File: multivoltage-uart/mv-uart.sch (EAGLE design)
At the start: 39 parts, among them SW1 DIP_SP6T, U1 IP4234CZ6, U2 CP2105-GM, U3 LDO_SHD_ADJ-AP2127K-ADJ, X1 MINI-USB-SHIELD-UX60-MB-5ST

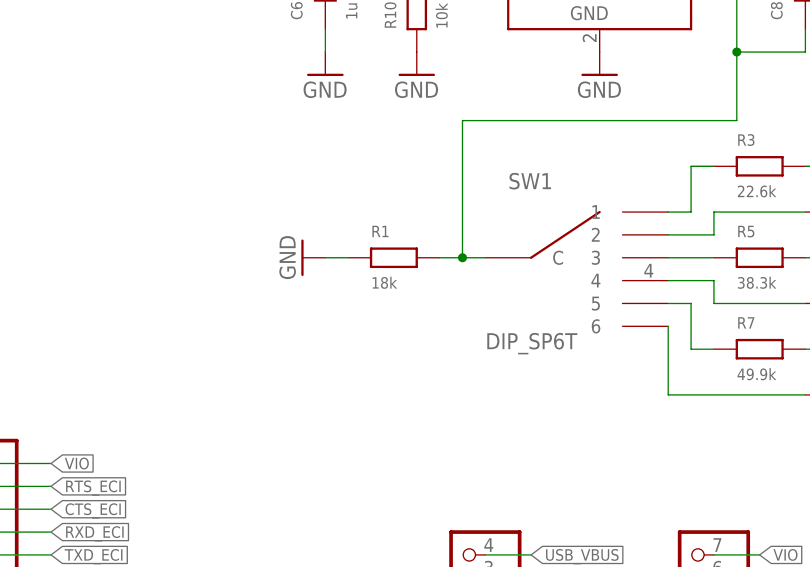
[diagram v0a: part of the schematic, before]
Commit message: mv-uart: Add digikey link for all major parts
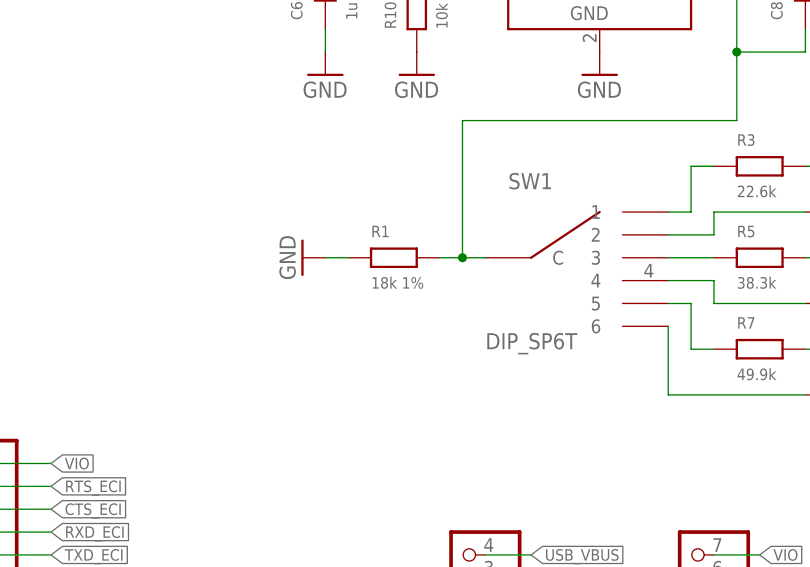
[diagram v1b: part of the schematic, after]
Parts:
- C1, C2, C3, C4, C5, C6, C7, C8, C9: CLASS (none) -> CAPACITOR; DESCRIPTION (none) -> NO DESCRIPTION; LINK (none) -> UNKNOWN LINK; MANUFACTURER (none) -> UNKNOWN MANUFACTURER; MANUFACTURERPARTNUMBER (none) -> UNKNOWN MANUFACTURER PART NUMBER; POPULATED (none) -> TRUE; ROHSCERTIFICATE (none) -> UNKNOWN ROHS CERTIFICATE; SOURCE (none) -> UNKNOWN SOURCE; SOURCEPARTNUMBER (none) -> UNKNOWN SOURCE PART NUMBER
- D1, D2: CLASS (none) -> DIODE; DESCRIPTION (none) -> NO DESCRIPTION; LINK (none) -> http://www.digikey.com/product-detail/en/wurth-electronics-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; MANUFACTURER (none) -> UNKNOWN MANUFACTURER; MANUFACTURERPARTNUMBER (none) -> UNKNOWN MANUFACTURER PART NUMBER; POPULATED (none) -> TRUE; ROHSCERTIFICATE (none) -> UNKNOWN ROHS CERTIFICATE; SOURCE (none) -> UNKNOWN SOURCE; SOURCEPARTNUMBER (none) -> UNKNOWN SOURCE PART NUMBER
- JP1, JP2, JP3, JP4, JP5: CLASS (none) -> CONNECTOR\JUMPER; DESCRIPTION (none) -> NO DESCRIPTION; LINK (none) -> UNKNOWN LINK; MANUFACTURER (none) -> UNKNOWN MANUFACTURER; MANUFACTURERPARTNUMBER (none) -> UNKNOWN MANUFACTURER PART NUMBER; POPULATED (none) -> TRUE; ROHSCERTIFICATE (none) -> UNKNOWN ROHS CERTIFICATE; SOURCE (none) -> UNKNOWN SOURCE; SOURCEPARTNUMBER (none) -> UNKNOWN SOURCE PART NUMBER
- R1: value 18k -> 18k 1%; CLASS (none) -> RESISTOR; DESCRIPTION (none) -> NO DESCRIPTION; LINK (none) -> http://www.digikey.com/product-detail/en/yageo/RC0603FR-071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; MANUFACTURER (none) -> UNKNOWN MANUFACTURER; MANUFACTURERPARTNUMBER (none) -> UNKNOWN MANUFACTURER PART NUMBER; POPULATED (none) -> TRUE; ROHSCERTIFICATE (none) -> UNKNOWN ROHS CERTIFICATE; SOURCE (none) -> UNKNOWN SOURCE; SOURCEPARTNUMBER (none) -> UNKNOWN SOURCE PART NUMBER
- R10, R11, R12, R13, R14, R15, R16, R17, R18, R2, R9: CLASS (none) -> RESISTOR; DESCRIPTION (none) -> NO DESCRIPTION; LINK (none) -> UNKNOWN LINK; MANUFACTURER (none) -> UNKNOWN MANUFACTURER; MANUFACTURERPARTNUMBER (none) -> UNKNOWN MANUFACTURER PART NUMBER; POPULATED (none) -> TRUE; ROHSCERTIFICATE (none) -> UNKNOWN ROHS CERTIFICATE; SOURCE (none) -> UNKNOWN SOURCE; SOURCEPARTNUMBER (none) -> UNKNOWN SOURCE PART NUMBER
- R3: CLASS (none) -> RESISTOR; DESCRIPTION (none) -> NO DESCRIPTION; LINK (none) -> http://www.digikey.com/product-detail/en/yageo/RC0603FR-072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; MANUFACTURER (none) -> UNKNOWN MANUFACTURER; MANUFACTURERPARTNUMBER (none) -> UNKNOWN MANUFACTURER PART NUMBER; POPULATED (none) -> TRUE; ROHSCERTIFICATE (none) -> UNKNOWN ROHS CERTIFICATE; SOURCE (none) -> UNKNOWN SOURCE; SOURCEPARTNUMBER (none) -> UNKNOWN SOURCE PART NUMBER
- R4, R5: CLASS (none) -> RESISTOR; DESCRIPTION (none) -> NO DESCRIPTION; LINK (none) -> http://www.digikey.com/product-detail/en/yageo/RC0603FR-073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; MANUFACTURER (none) -> UNKNOWN MANUFACTURER; MANUFACTURERPARTNUMBER (none) -> UNKNOWN MANUFACTURER PART NUMBER; POPULATED (none) -> TRUE; ROHSCERTIFICATE (none) -> UNKNOWN ROHS CERTIFICATE; SOURCE (none) -> UNKNOWN SOURCE; SOURCEPARTNUMBER (none) -> UNKNOWN SOURCE PART NUMBER
- R6, R7: CLASS (none) -> RESISTOR; DESCRIPTION (none) -> NO DESCRIPTION; LINK (none) -> http://www.digikey.com/product-detail/en/yageo/RC0603FR-074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; MANUFACTURER (none) -> UNKNOWN MANUFACTURER; MANUFACTURERPARTNUMBER (none) -> UNKNOWN MANUFACTURER PART NUMBER; POPULATED (none) -> TRUE; ROHSCERTIFICATE (none) -> UNKNOWN ROHS CERTIFICATE; SOURCE (none) -> UNKNOWN SOURCE; SOURCEPARTNUMBER (none) -> UNKNOWN SOURCE PART NUMBER
- R8: CLASS (none) -> RESISTOR; DESCRIPTION (none) -> NO DESCRIPTION; LINK (none) -> http://www.digikey.com/product-detail/en/yageo/RC0603FR-075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; MANUFACTURER (none) -> UNKNOWN MANUFACTURER; MANUFACTURERPARTNUMBER (none) -> UNKNOWN MANUFACTURER PART NUMBER; POPULATED (none) -> TRUE; ROHSCERTIFICATE (none) -> UNKNOWN ROHS CERTIFICATE; SOURCE (none) -> UNKNOWN SOURCE; SOURCEPARTNUMBER (none) -> UNKNOWN SOURCE PART NUMBER
- SW1: CLASS (none) -> UNKNOWN CLASS; DESCRIPTION (none) -> NO DESCRIPTION; LINK (none) -> UNKNOWN LINK; MANUFACTURER (none) -> UNKNOWN MANUFACTURER; MANUFACTURERPARTNUMBER (none) -> UNKNOWN MANUFACTURER PART NUMBER; POPULATED (none) -> TRUE; ROHSCERTIFICATE (none) -> UNKNOWN ROHS CERTIFICATE; SOURCE (none) -> UNKNOWN SOURCE; SOURCEPARTNUMBER (none) -> UNKNOWN SOURCE PART NUMBER
- U1: CLASS (none) -> IC; DESCRIPTION (none) -> NO DESCRIPTION; LINK (none) -> http://www.digikey.com/product-detail/en/nxp-semiconductors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; MANUFACTURER (none) -> UNKNOWN MANUFACTURER; MANUFACTURERPARTNUMBER (none) -> UNKNOWN MANUFACTURER PART NUMBER; POPULATED (none) -> TRUE; ROHSCERTIFICATE (none) -> UNKNOWN ROHS CERTIFICATE; SOURCE (none) -> UNKNOWN SOURCE; SOURCEPARTNUMBER (none) -> UNKNOWN SOURCE PART NUMBER
- U2: CLASS (none) -> IC; DESCRIPTION (none) -> NO DESCRIPTION; LINK (none) -> http://www.digikey.com/product-detail/en/silicon-labs/CP210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; MANUFACTURER (none) -> UNKNOWN MANUFACTURER; MANUFACTURERPARTNUMBER (none) -> UNKNOWN MANUFACTURER PART NUMBER; POPULATED (none) -> TRUE; ROHSCERTIFICATE (none) -> UNKNOWN ROHS CERTIFICATE; SOURCE (none) -> UNKNOWN SOURCE; SOURCEPARTNUMBER (none) -> UNKNOWN SOURCE PART NUMBER
- U3: CLASS (none) -> IC; DESCRIPTION (none) -> NO DESCRIPTION; LINK (none) -> http://www.digikey.com/product-detail/en/diodes-incorporate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; MANUFACTURER (none) -> UNKNOWN MANUFACTURER; MANUFACTURERPARTNUMBER (none) -> UNKNOWN MANUFACTURER PART NUMBER; POPULATED (none) -> TRUE; ROHSCERTIFICATE (none) -> UNKNOWN ROHS CERTIFICATE; SOURCE (none) -> UNKNOWN SOURCE; SOURCEPARTNUMBER (none) -> UNKNOWN SOURCE PART NUMBER
- X1: CLASS (none) -> CONNECTOR; DESCRIPTION (none) -> NO DESCRIPTION; LINK (none) -> http://www.digikey.com/product-detail/en/hirose-electric-co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; MANUFACTURER (none) -> UNKNOWN MANUFACTURER; MANUFACTURERPARTNUMBER (none) -> UNKNOWN MANUFACTURER PART NUMBER; POPULATED (none) -> TRUE; ROHSCERTIFICATE (none) -> UNKNOWN ROHS CERTIFICATE; SOURCE (none) -> UNKNOWN SOURCE; SOURCEPARTNUMBER (none) -> UNKNOWN SOURCE PART NUMBER

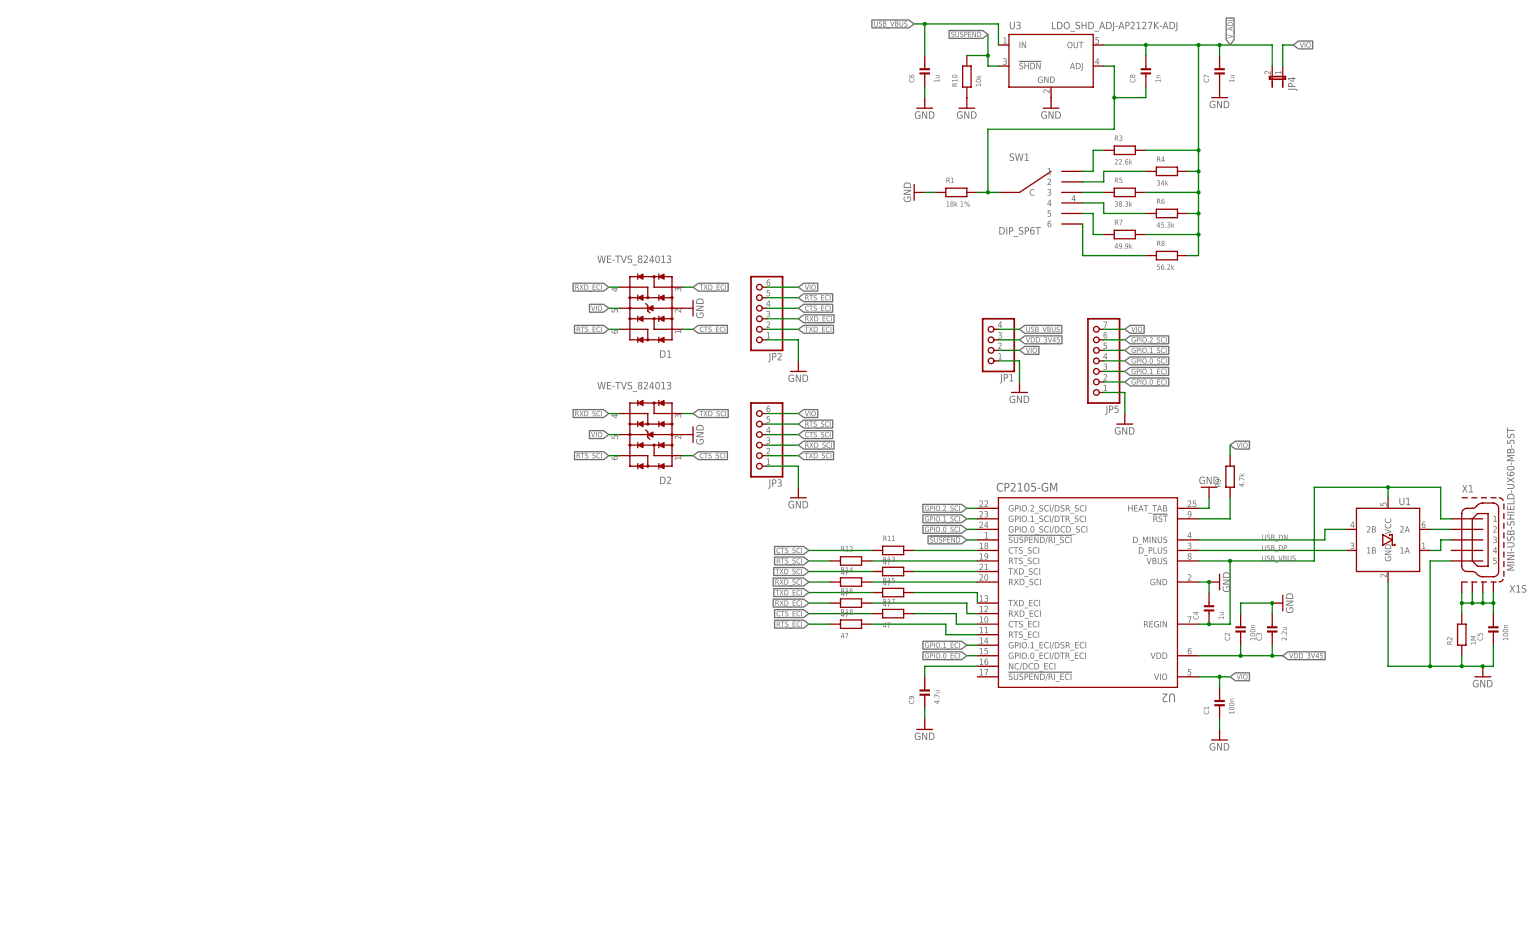
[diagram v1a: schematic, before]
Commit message: mv-uart: Beatify schematics + Add comments
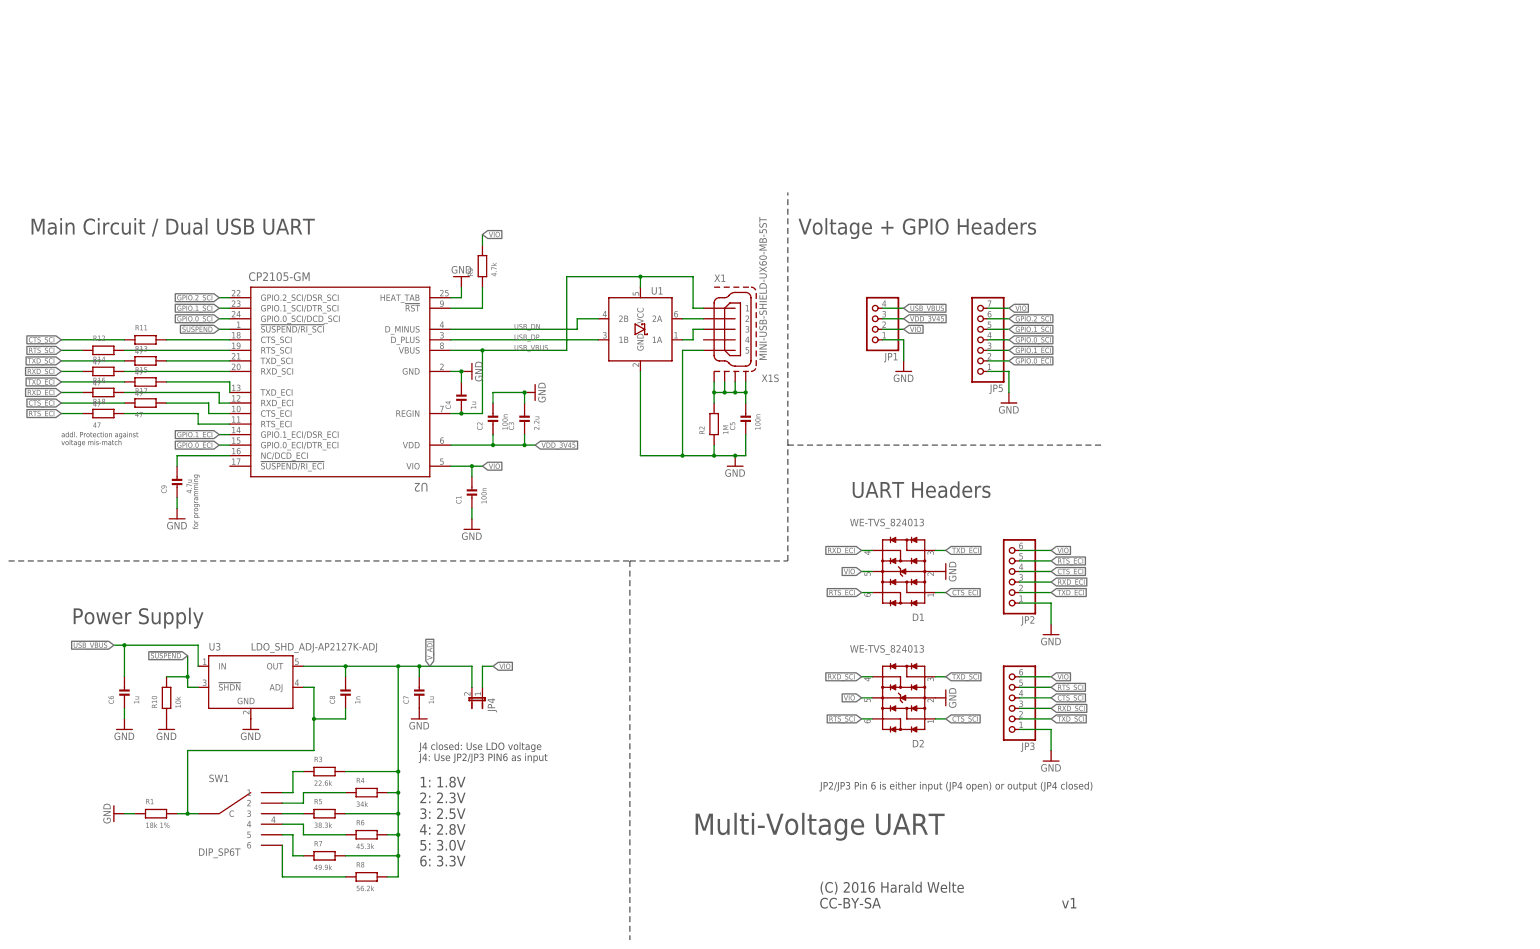
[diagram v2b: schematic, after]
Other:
- note added: "(C) 2016 Harald Welte CC-BY-SA"
- note added: "1: 1.8V 2: 2.3V 3: 2.5V 4: 2.8V 5: 3.0V 6: 3.3V"
- note added: "J4 closed: Use LDO voltage J4: Use JP2/JP3 PIN6 as input"
- note added: "JP2/JP3 Pin 6 is either input (JP4 open) or output (JP4 closed)"
- note added: "Main Circuit / Dual USB UART"
- note added: "Multi-Voltage UART"
- note added: "Power Supply"
- note added: "UART Headers"
- note added: "Voltage + GPIO Headers"
- note added: "addl. Protection against voltage mis-match"
- note added: "for programming"
- moved on the sheet: C1, C2, C3, C4, C5, C6, C7, C8, C9, D1, D2, JP1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

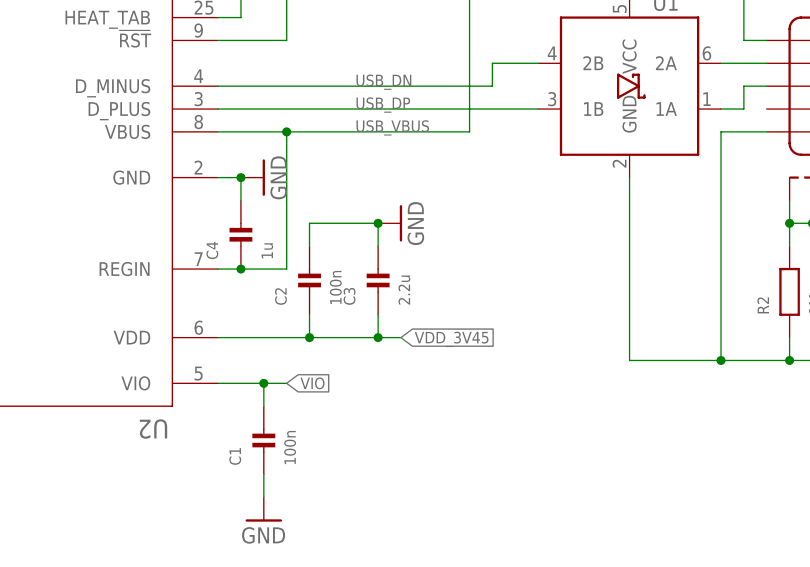
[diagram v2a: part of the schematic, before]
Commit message: Complete BOM attributes + export BOM
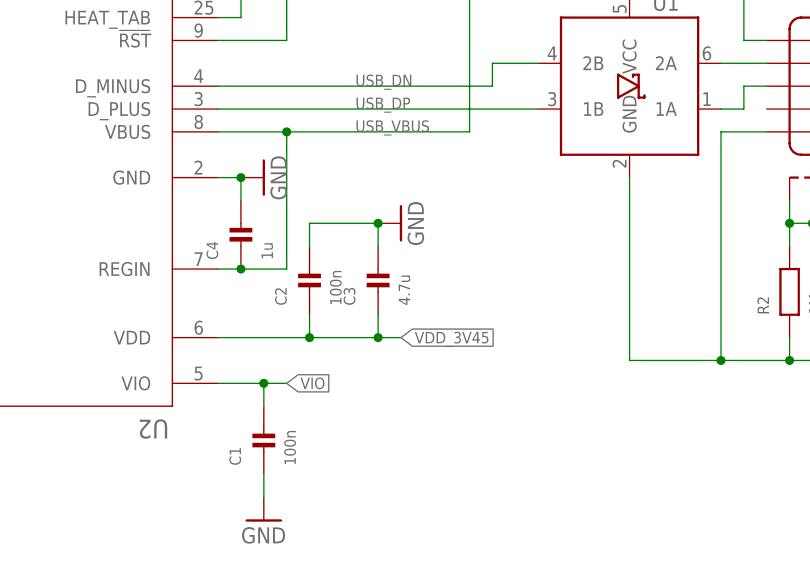
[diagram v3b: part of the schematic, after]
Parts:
- C1, C2, C5: DESCRIPTION NO DESCRIPTION -> 0.10µF 16V Ceramic Capacitor X5R 0201 (0603 Metric) 0.024" 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; LINK UNKNOWN LINK -> http://www.digikey.com/product-detail/en/murata-electronics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; MANUFACTURER UNKNOWN MANUFACTURER -> Murata Electronics North America; MANUFACTURERPARTNUMBER UNKNOWN MANUFACTURER PART NUMBER -> GRM033R61C104KE84D; SOURCE UNKNOWN SOURCE -> DIGIKEY; SOURCEPARTNUMBER UNKNOWN SOURCE PART NUMBER -> 490-9985-1-ND
- C3: value 2.2u -> 4.7u; DESCRIPTION NO DESCRIPTION -> 4.7µF 10V Ceramic Capacitor X5R 0603 (1608 Metric) 0.063" L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; LINK UNKNOWN LINK -> http://www.digikey.com/product-detail/en/samsung-electro-me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; MANUFACTURER UNKNOWN MANUFACTURER -> Samsung Electro-Mechanics America, Inc.; MANUFACTURERPARTNUMBER UNKNOWN MANUFACTURER PART NUMBER -> CL10A475KP8NNNC; SOURCE UNKNOWN SOURCE -> DIGIKEY; SOURCEPARTNUMBER UNKNOWN SOURCE PART NUMBER -> 1276-1044-1-ND
- C4, C6, C7: DESCRIPTION NO DESCRIPTION -> 1µF 16V Ceramic Capacitor X5R 0603 (1608 Metric) 0.063" L x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; LINK UNKNOWN LINK -> http://www.digikey.com/product-detail/en/murata-electronics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; MANUFACTURER UNKNOWN MANUFACTURER -> Murata Electronics North America; MANUFACTURERPARTNUMBER UNKNOWN MANUFACTURER PART NUMBER -> GRM188R61C105KA93J; SOURCE UNKNOWN SOURCE -> DIGIKEY; SOURCEPARTNUMBER UNKNOWN SOURCE PART NUMBER -> 490-6412-1-ND
- C8: DESCRIPTION NO DESCRIPTION -> 1000pF 100V Ceramic Capacitor X7R 0603 (1608 Metric) 0.063"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; LINK UNKNOWN LINK -> http://www.digikey.com/product-detail/en/samsung-electro-me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; MANUFACTURER UNKNOWN MANUFACTURER -> Samsung Electro-Mechanics America, Inc.; MANUFACTURERPARTNUMBER UNKNOWN MANUFACTURER PART NUMBER -> CL10B102KC8NNNC; SOURCE UNKNOWN SOURCE -> DIGIKEY; SOURCEPARTNUMBER UNKNOWN SOURCE PART NUMBER -> 1276-1131-1-ND
- C9: DESCRIPTION NO DESCRIPTION -> 4.7µF 10V Ceramic Capacitor X5R 0603 (1608 Metric) 0.063" L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; LINK UNKNOWN LINK -> http://www.digikey.com/product-detail/en/samsung-electro-me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; MANUFACTURER UNKNOWN MANUFACTURER -> Samsung Electro-Mechanics America, Inc.; MANUFACTURERPARTNUMBER UNKNOWN MANUFACTURER PART NUMBER -> CL10A475KP8NNNC; SOURCE UNKNOWN SOURCE -> DIGIKEY; SOURCEPARTNUMBER UNKNOWN SOURCE PART NUMBER -> 1276-1044-1-ND
- D1, D2: DESCRIPTION NO DESCRIPTION -> TVS DIODE 3.3VWM 6VC SOT23; MANUFACTURER UNKNOWN MANUFACTURER -> Wurth Electronics Inc; MANUFACTURERPARTNUMBER UNKNOWN MANUFACTURER PART NUMBER -> 824013; SOURCE UNKNOWN SOURCE -> DIGIKEY; SOURCEPARTNUMBER UNKNOWN SOURCE PART NUMBER -> 732-4466-1-ND
- R1: DESCRIPTION NO DESCRIPTION -> RES SMD 18K OHM 1% 1/10W 0603; MANUFACTURER UNKNOWN MANUFACTURER -> Yageo; MANUFACTURERPARTNUMBER UNKNOWN MANUFACTURER PART NUMBER -> RC0603FR-0718KL; SOURCE UNKNOWN SOURCE -> DIGIKEY; SOURCEPARTNUMBER UNKNOWN SOURCE PART NUMBER -> 311-18.0KHRCT-ND
- R10: DESCRIPTION NO DESCRIPTION -> RES SMD 10K OHM 5% 1/10W 0603; LINK UNKNOWN LINK -> http://www.digikey.com/product-detail/en/samsung-electro-me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; MANUFACTURER UNKNOWN MANUFACTURER -> Samsung Electro-Mechanics America, Inc.; MANUFACTURERPARTNUMBER UNKNOWN MANUFACTURER PART NUMBER -> RC1608J103CS; SOURCE UNKNOWN SOURCE -> DIGIKEY; SOURCEPARTNUMBER UNKNOWN SOURCE PART NUMBER -> 1276-5086-1-ND
- R11, R12, R13, R14, R15, R16, R17, R18: DESCRIPTION NO DESCRIPTION -> RES SMD 47 OHM 5% 1/10W 0603; LINK UNKNOWN LINK -> http://www.digikey.com/product-detail/en/yageo/RC0603JR-074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; MANUFACTURER UNKNOWN MANUFACTURER -> Yageo; MANUFACTURERPARTNUMBER UNKNOWN MANUFACTURER PART NUMBER -> RC0603JR-0747RL; SOURCE UNKNOWN SOURCE -> DIGIKEY; SOURCEPARTNUMBER UNKNOWN SOURCE PART NUMBER -> 311-47GRCT-ND
- R2: DESCRIPTION NO DESCRIPTION -> RES SMD 1M OHM 5% 1/20W 0201; LINK UNKNOWN LINK -> http://www.digikey.com/product-detail/en/samsung-electro-me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; MANUFACTURER UNKNOWN MANUFACTURER -> Samsung Electro-Mechanics America, Inc.; MANUFACTURERPARTNUMBER UNKNOWN MANUFACTURER PART NUMBER -> RC0603J105CS; SOURCE UNKNOWN SOURCE -> DIGIKEY; SOURCEPARTNUMBER UNKNOWN SOURCE PART NUMBER -> 1276-3856-1-ND
- R3: DESCRIPTION NO DESCRIPTION -> RES SMD 22.6K OHM 1% 1/10W 0603; MANUFACTURER UNKNOWN MANUFACTURER -> Yageo; MANUFACTURERPARTNUMBER UNKNOWN MANUFACTURER PART NUMBER -> RC0603FR-0722K6L; SOURCE UNKNOWN SOURCE -> DIGIKEY; SOURCEPARTNUMBER UNKNOWN SOURCE PART NUMBER -> 311-22.6KHRCT-ND
- R4: DESCRIPTION NO DESCRIPTION -> RES SMD 34K OHM 1% 1/10W 0603; MANUFACTURER UNKNOWN MANUFACTURER -> Yageo; MANUFACTURERPARTNUMBER UNKNOWN MANUFACTURER PART NUMBER -> RC0603FR-0734KL; SOURCE UNKNOWN SOURCE -> DIGIKEY; SOURCEPARTNUMBER UNKNOWN SOURCE PART NUMBER -> 311-34.0KHRCT-ND
- R5: DESCRIPTION NO DESCRIPTION -> RES SMD 38.3K OHM 1% 1/10W 0603; MANUFACTURER UNKNOWN MANUFACTURER -> Yageo; MANUFACTURERPARTNUMBER UNKNOWN MANUFACTURER PART NUMBER -> RC0603FR-0738K3L; SOURCE UNKNOWN SOURCE -> DIGIKEY; SOURCEPARTNUMBER UNKNOWN SOURCE PART NUMBER -> 311-38.3KHRCT-ND
- R6: DESCRIPTION NO DESCRIPTION -> RES SMD 45.3K OHM 1% 1/10W 0603; MANUFACTURER UNKNOWN MANUFACTURER -> Yageo; MANUFACTURERPARTNUMBER UNKNOWN MANUFACTURER PART NUMBER -> RC0603FR-0745K3L; SOURCE UNKNOWN SOURCE -> DIGIKEY; SOURCEPARTNUMBER UNKNOWN SOURCE PART NUMBER -> 311-45.3KHRCT-ND
- R7: DESCRIPTION NO DESCRIPTION -> RES SMD 49.9K OHM 1% 1/10W 0603; MANUFACTURER UNKNOWN MANUFACTURER -> Yageo; MANUFACTURERPARTNUMBER UNKNOWN MANUFACTURER PART NUMBER -> RC0603FR-0749K9L; SOURCE UNKNOWN SOURCE -> DIGIKEY; SOURCEPARTNUMBER UNKNOWN SOURCE PART NUMBER -> 311-49.9KHRCT-ND
- R8: DESCRIPTION NO DESCRIPTION -> RES SMD 56.2K OHM 1% 1/10W 0603; MANUFACTURER UNKNOWN MANUFACTURER -> Yageo; MANUFACTURERPARTNUMBER UNKNOWN MANUFACTURER PART NUMBER -> RC0603FR-0756K2L; SOURCE UNKNOWN SOURCE -> DIGIKEY; SOURCEPARTNUMBER UNKNOWN SOURCE PART NUMBER -> 311-56.2KHRCT-ND
- R9: DESCRIPTION NO DESCRIPTION -> RES SMD 4.7K OHM 5% 1/10W 0603; LINK UNKNOWN LINK -> http://www.digikey.com/product-detail/en/yageo/RC0603JR-074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; MANUFACTURER UNKNOWN MANUFACTURER -> Yageo; MANUFACTURERPARTNUMBER UNKNOWN MANUFACTURER PART NUMBER -> RC0603JR-074K7L; SOURCE UNKNOWN SOURCE -> DIGIKEY; SOURCEPARTNUMBER UNKNOWN SOURCE PART NUMBER -> 311-4.7KGRCT-ND
- SW1: DESCRIPTION NO DESCRIPTION -> Dip Switch SP6T 6 Position Through Hole Rotary with Shaft A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; LINK UNKNOWN LINK -> http://www.digikey.com/product-detail/en/copal-electronics-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; MANUFACTURER UNKNOWN MANUFACTURER -> Copal Electronics Inc.; MANUFACTURERPARTNUMBER UNKNOWN MANUFACTURER PART NUMBER -> SS-10-16NP-LE; SOURCE UNKNOWN SOURCE -> DIGIKEY; SOURCEPARTNUMBER UNKNOWN SOURCE PART NUMBER -> 563-1080-ND
- U1: DESCRIPTION NO DESCRIPTION -> TVS DIODE 5.5VWM 6TSOP; MANUFACTURER UNKNOWN MANUFACTURER -> NXP Semiconductors; MANUFACTURERPARTNUMBER UNKNOWN MANUFACTURER PART NUMBER -> IP4234CZ6,125; SOURCE UNKNOWN SOURCE -> DIGIKEY; SOURCEPARTNUMBER UNKNOWN SOURCE PART NUMBER -> 568-5869-1-ND
- U2: DESCRIPTION NO DESCRIPTION -> USB Bridge, USB to UART USB 2.0 UART Interface 24-QFN (4x4); MANUFACTURER UNKNOWN MANUFACTURER -> Silicon Labs; MANUFACTURERPARTNUMBER UNKNOWN MANUFACTURER PART NUMBER -> CP2105-F01-GM; SOURCE UNKNOWN SOURCE -> DIGIKEY; SOURCEPARTNUMBER UNKNOWN SOURCE PART NUMBER -> 336-2009-5-ND
- U3: DESCRIPTION NO DESCRIPTION -> Linear Voltage Regulator IC Positive Adjustable 1 Output 0.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; MANUFACTURER UNKNOWN MANUFACTURER -> Diodes Incorporated; MANUFACTURERPARTNUMBER UNKNOWN MANUFACTURER PART NUMBER -> AP2127K-ADJTRG1; SOURCE UNKNOWN SOURCE -> DIGIKEY; SOURCEPARTNUMBER UNKNOWN SOURCE PART NUMBER -> AP2127K-ADJTRG1DICT-ND
- X1: DESCRIPTION NO DESCRIPTION -> USB - mini B USB 2.0 Receptacle Connector 5 Position Surfac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; MANUFACTURER UNKNOWN MANUFACTURER -> Hirose Electric Co Ltd; MANUFACTURERPARTNUMBER UNKNOWN MANUFACTURER PART NUMBER -> UX60-MB-5ST; SOURCE UNKNOWN SOURCE -> DIGIKEY; SOURCEPARTNUMBER UNKNOWN SOURCE PART NUMBER -> H2959CT-ND
